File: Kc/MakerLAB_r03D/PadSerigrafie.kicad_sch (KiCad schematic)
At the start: 20 parts

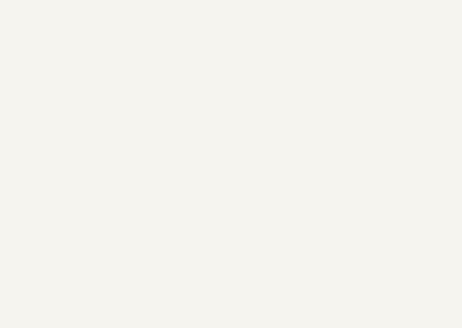
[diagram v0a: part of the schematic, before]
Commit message: Con Supporto Breadboard
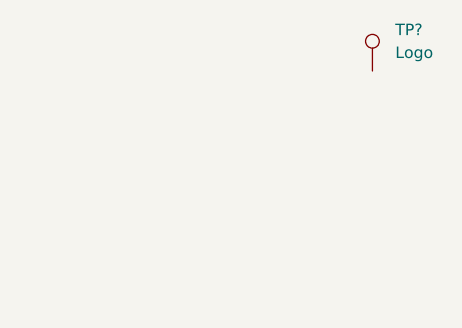
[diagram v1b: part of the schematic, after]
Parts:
- added TP?: Logo, Logo Einstein:Einstein Logo, symbol Connector:TestPoint
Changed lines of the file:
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@@
+    (pin "1")
+  )
+  (symbol (lib_id "Connector:TestPoint") (at 226.06 60.96 0) (unit 1)
+    (in_bom yes) (on_board yes) (fields_autoplaced)
+    (property "Reference" "TP?" (id 0) (at 228.6 56.3879 0)
+      (effects (font (size 1.27 1.27)) (justify left))
+    )
+    (property "Value" "Logo" (id 1) (at 228.6 58.9279 0)
+      (effects (font (size 1.27 1.27)) (justify left))
+    )
+    (property "Footprint" "Logo Einstein:Einstein Logo" (id 2) (at 231.14 60.96 0)
+      (effects (font (size 1.27 1.27)) hide)
+    )
+    (property "Datasheet" "~" (id 3) (at 231.14 60.96 0)
+      (effects (font (size 1.27 1.27)) hide)
+    )
     (pin "1")
   )
